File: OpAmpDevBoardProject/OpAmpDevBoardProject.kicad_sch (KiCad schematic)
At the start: 62 parts, among them J101 Conn_01x07, SW101 SW_SPST, SW102 SW_SPST, SW103 SW_SPST, SW104 SW_SPST, SW105 SW_SPST, SW106 SW_SPST, SW107 SW_SPST, SW108 SW_SPST, SW109 SW_SPST, SW110 SW_SPST, SW111 SW_SPST, SW112 SW_SPST, SW113 SW_SPST, SW114 SW_SPST, SW115 SW_SPST, SW116 SW_SPST, SW117 SW_SPST, SW118 SW_SPST, SW119 SW_SPST, SW120 SW_SPST, SW121 SW_SPST, SW122 SW_SPST, SW123 SW_SPST, SW124 SW_SPST, SW125 SW_SPST, SW126 SW_SPST, SW127 SW_SPST, SW128 SW_SPST, SW129 SW_SPST, SW130 SW_SPST, SW131 SW_SPST, SW132 SW_SPST, SW133 SW_SPST, SW134 SW_SPST, SW135 SW_SPST, SW136 SW_SPST, SW137 SW_SPST, SW138 SW_SPST, U101 DoualOutOpAmpGeneric

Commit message: finished botzh sides
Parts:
- added H101, H102, H103, H104: MountingHole, OpampDeVBoard_Foot_Lib:Spacer, symbol Mechanical:MountingHole
- added J102, J103, J104, J105, J106, J107, J108, J112, J113, J114, J115, J117, J118, J119, J120, J122, J123, J124, J125, J126, J127, J128: Conn_01x01_Pin, Connector_PinHeader_2.54mm:PinHeader_1x01_P2.54mm_Vertical, symbol Connector:Conn_01x01_Pin
- added J109: Conn_01x07_Socket, Connector_PinHeader_2.54mm:PinHeader_1x07_P2.54mm_Vertical, symbol Connector:Conn_01x07_Socket
- added J110, J111, J116, J121: 227161-2, OpAmpDevBoard_Mouser:2271612, symbol OpAmpBoard_Mouser:227161-2
- added RV103, RV104, RV106, RV107: R_Potentiometer, OpampDeVBoard_Foot_Lib:PTV09A-1_Vertical, symbol Device:R_Potentiometer
- added SW139, SW140, SW141, SW142, SW143, SW144, SW145, SW146: SW_SPST, OpAmpDevBoard_Mouser:SS12SDP2, symbol Switch:SW_SPST
- C101, C102, C103, C104, C105, C106, C107, C108: footprint (none) -> Capacitor_SMD:C_0805_2012Metric_Pad1.18x1.45mm_HandSolder
- J101: footprint (none) -> Connector_PinSocket_2.54mm:PinSocket_1x07_P2.54mm_Vertical
- R101, R102, R103, R104, R105, R106, R107, R108, R109, R110, R111, R112: footprint (none) -> Resistor_SMD:R_0805_2012Metric_Pad1.20x1.40mm_HandSolder
- RV101, RV102: footprint (none) -> OpampDeVBoard_Foot_Lib:PTV09A-1_Vertical
- SW101, SW102, SW103, SW104, SW105, SW106, SW107, SW108, SW109, SW110, SW111, SW112, SW113, SW114, SW115, SW116, SW117, SW118, SW119, SW120, SW121, SW122, SW123, SW124, SW125, SW126, SW127, SW128, SW129, SW130, SW131, SW132, SW133, SW134, SW135, SW136, SW137, SW138: footprint (none) -> OpAmpDevBoard_Mouser:SS12SDP2
- U101: footprint (none) -> OpampDeVBoard_Foot_Lib:OpAmpBoardConnector
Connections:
- net GND: now also J101.2 (Pin_2), J109.2 (Pin_2), J110.2 (Ground), J110.MH1, J110.MH2, J111.2 (Ground), J111.MH1, J111.MH2, J116.2 (Ground), J116.MH1, J116.MH2, J121.2 (Ground), J121.MH1, J121.MH2, J122.1 (Pin_1), J123.1 (Pin_1), RV103.3, RV104.3, RV106.3, RV107.3
- net at C104.2, R106.2, SW129.2 (B)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: now also J116.1 (Signal), J117.1 (Pin_1), J118.1 (Pin_1)
- net at C101.1, C105.2, R101.1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: now also J102.1 (Pin_1), J107.1 (Pin_1), J108.1 (Pin_1)
- net at R107.1: now also SW141.2 (B); no longer SW133.1 (A)
- net at R107.2, SW117.2 (B), SW118.2 (B)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: now also J105.1 (Pin_1), RV103.2, SW140.1 (A), SW144.1 (A); no longer R108.1
- net at C102.2, C108.1, R112.1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: now also J103.1 (Pin_1), J127.1 (Pin_1), J128.1 (Pin_1)
- net at C102.1, R104.2, SW111.2 (B)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: now also J126.1 (Pin_1), RV107.2
- net at R103.2, SW113.2 (B), SW114.2 (B)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: now also J125.1 (Pin_1), RV106.2, SW143.1 (A), SW146.1 (A); no longer R104.1
- net at C105.1, R108.2, SW119.2 (B)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: now also J106.1 (Pin_1), RV104.2
- net at SW136.1 (A): now also J110.1 (Signal), J112.1 (Pin_1), J113.1 (Pin_1), J124.1 (Pin_1), SW142.1 (A), SW145.1 (A); no longer R103.1
- net at C107.2, R110.2, SW101.2 (B)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: now also J119.1 (Pin_1), J120.1 (Pin_1), J121.1 (Signal)
- net V+: now reaches J101.1 (Pin_1)
- net V+: now also U101.8 (V+), J109.1 (Pin_1)
- net V-: now reaches J101.3 (Pin_3)
- net V-: now also U101.5 (V-), J109.3 (Pin_3)
- net Act: now reaches J101.4 (Pin_4)
- net Act: now also U101.9 (Act), J109.4 (Pin_4)
- net Sleep: now reaches J101.5 (Pin_5)
- net Sleep: now also U101.10 (Sleep), J109.5 (Pin_5)
- net Div1: now reaches J101.6 (Pin_6)
- net Div1: now also U101.3 (Div1), J109.6 (Pin_6)
- net Div2: now reaches J101.7 (Pin_7)
- net Div2: now also U101.4 (Div2), J109.7 (Pin_7)
- new net: RV103.1, SW139.2 (B)
- new net: R108.1, SW144.2 (B)
- new net: J104.1 (Pin_1), J111.1 (Signal), J114.1 (Pin_1), J115.1 (Pin_1), SW133.1 (A), SW139.1 (A), SW141.1 (A)
- new net: R104.1, SW146.2 (B)
- new net: RV104.1, SW140.2 (B)
- new net: RV107.1, SW143.2 (B)
- new net: R103.1, SW145.2 (B)
- new net: RV106.1, SW142.2 (B)
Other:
- moved on the sheet: C101, C102, C103, C104, C105, C106, C107, C108, J101, R101, R102, R103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

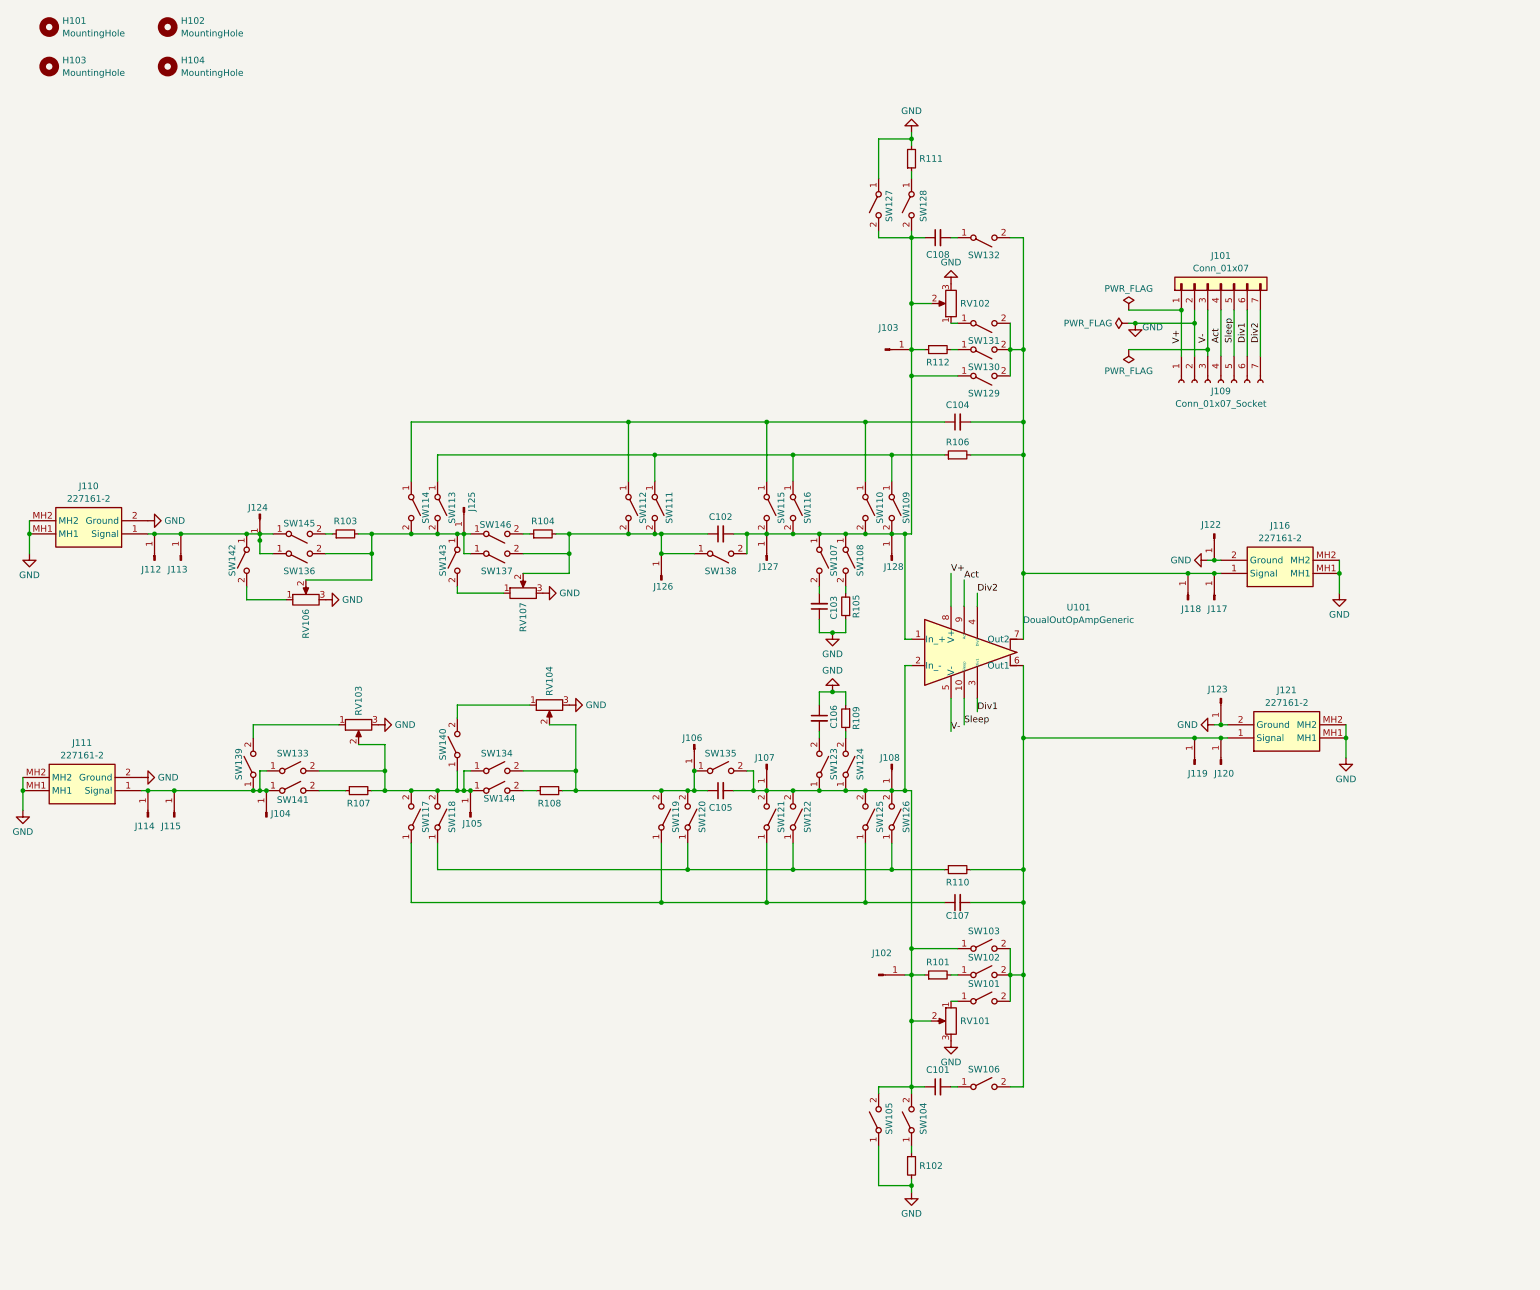
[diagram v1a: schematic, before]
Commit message: added double switch and started changing schematic
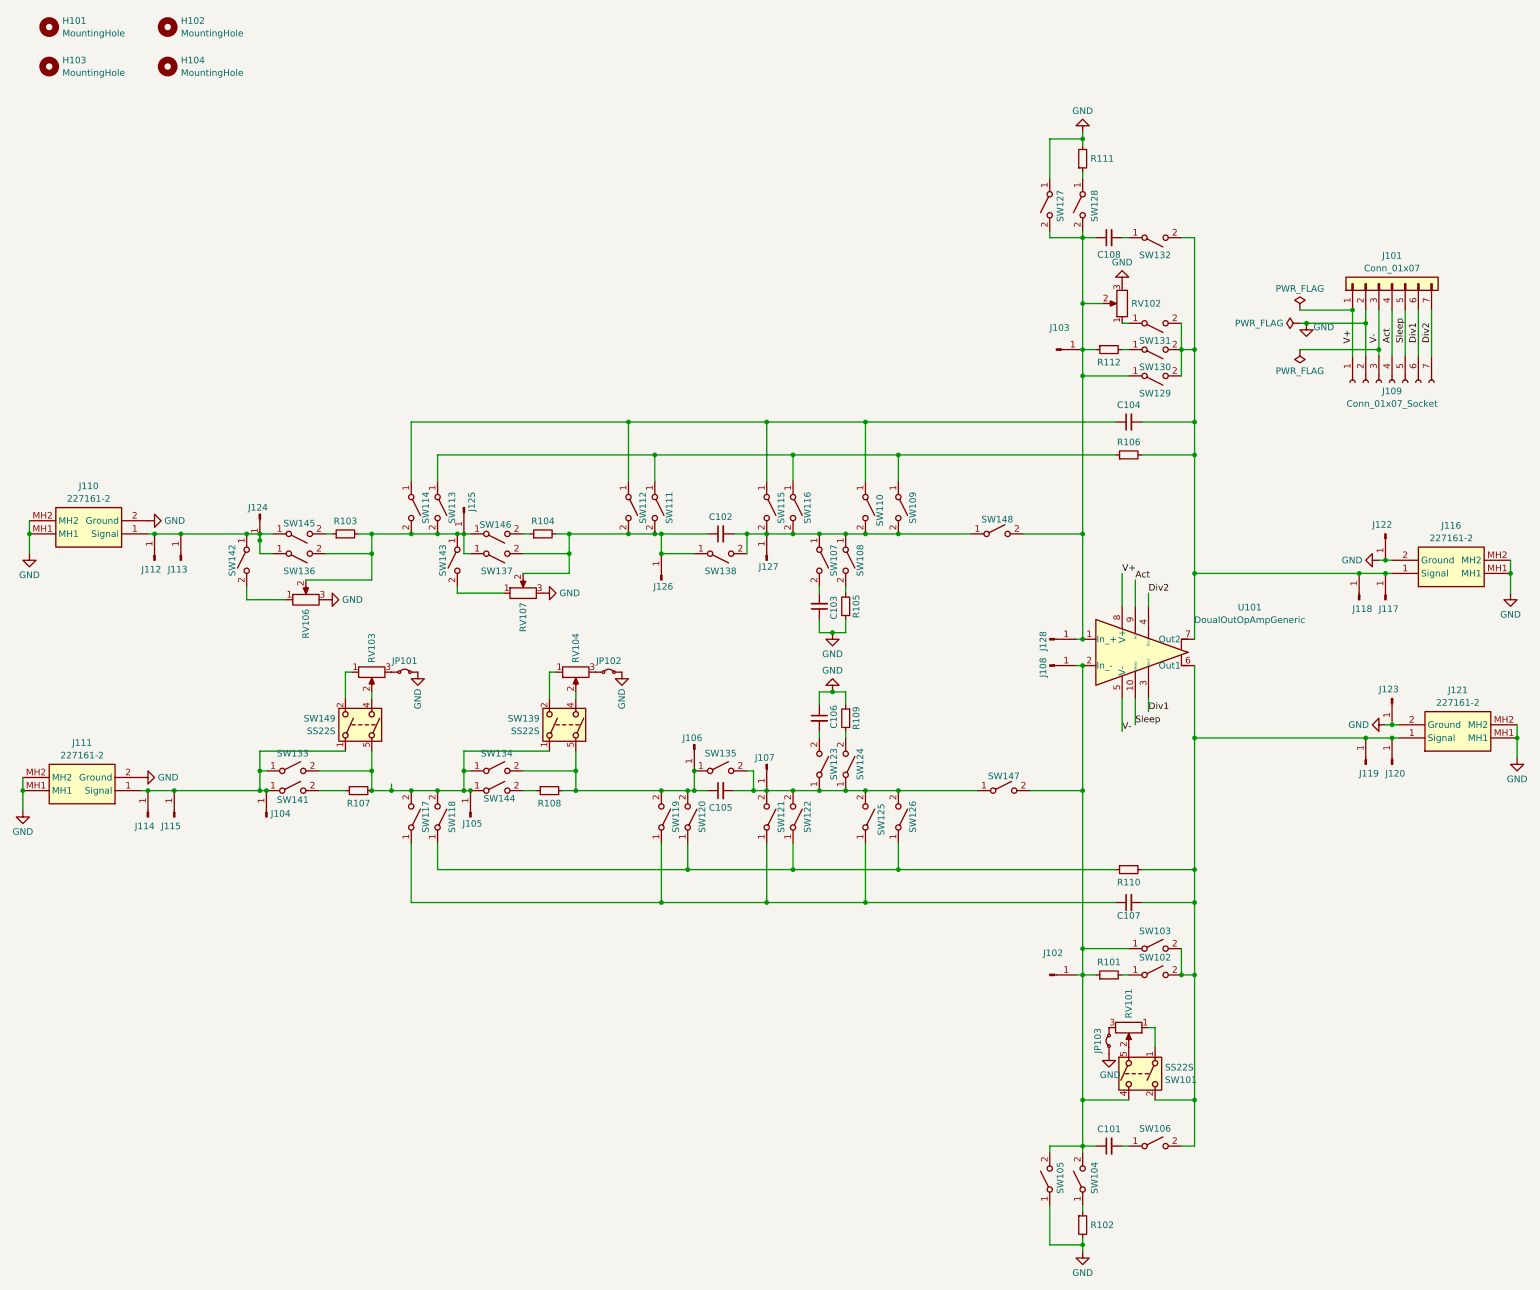
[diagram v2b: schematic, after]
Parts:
- removed SW101, SW139, SW140: SW_SPST, OpAmpDevBoard_Mouser:SS12SDP2, symbol Switch:SW_SPST
- added JP101, JP102, JP103: Jumper_2_Small_Bridged, symbol Jumper:Jumper_2_Small_Bridged
- added SW101, SW139, SW149: SS22S, OpAmpDevBoard_Mouser:SS22SDP2, symbol DiverseOpAmps:SS22S
- added SW147, SW148: SW_SPST, OpAmpDevBoard_Mouser:SS12SDP2, symbol Switch:SW_SPST
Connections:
- net GND: now also JP101.2 (B), JP102.2 (B), JP103.1 (A); no longer RV101.3, RV103.3, RV104.3
- net at C105.2, J107.1 (Pin_1), SW121.2 (B)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: now also SW147.1 (A); no longer C101.1, J102.1 (Pin_1), J108.1 (Pin_1), R101.1, RV101.2, SW103.1 (A), SW104.2 (B), SW105.2 (B), U101.2 (In_-)
- net at C102.2, J127.1 (Pin_1), SW107.1 (A)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: now also SW148.1 (A); no longer C108.1, J103.1 (Pin_1), J128.1 (Pin_1), R112.1, RV102.2, SW127.2 (B), SW128.2 (B), SW129.1 (A), U101.1 (In_+)
- net at J105.1 (Pin_1), R107.2, SW117.2 (B)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: now also SW139.1, SW149.5; no longer RV103.2
- net at C107.2, J119.1 (Pin_1), J120.1 (Pin_1)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: now also SW101.2
- net at RV103.1: now also SW149.2
- net at C105.1, J106.1 (Pin_1), R108.2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: now also SW139.5; no longer RV104.2
- net at RV101.1: now also SW101.1
- net at J104.1 (Pin_1), J111.1 (Signal), J114.1 (Pin_1)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: now also SW149.1
- net at RV104.1: now also SW139.2
- new net: C101.1, J102.1 (Pin_1), J108.1 (Pin_1), R101.1, SW101.4, SW103.1 (A), SW104.2 (B), SW105.2 (B), SW147.2 (B), U101.2 (In_-)
- new net: C108.1, J103.1 (Pin_1), J128.1 (Pin_1), R112.1, RV102.2, SW127.2 (B), SW128.2 (B), SW129.1 (A), SW148.2 (B), U101.1 (In_+)
- new net: RV103.2, SW149.4
- new net: JP101.1 (A), RV103.3
- new net: RV101.2, SW101.5
- new net: JP103.2 (B), RV101.3
- new net: RV104.2, SW139.4
- new net: JP102.1 (A), RV104.3
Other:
- moved on the sheet: C101, C104, C107, C108, J101, J102, J103, J108, J109, J116, J117, J118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

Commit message: late night fu me
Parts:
- removed SW131, SW142, SW143: SW_SPST, OpAmpDevBoard_Mouser:SS12SDP2, symbol Switch:SW_SPST
- added JP104, JP105, JP106: Jumper_2_Small_Bridged, Connector_PinHeader_2.54mm:PinHeader_1x02_P2.54mm_Vertical, symbol Jumper:Jumper_2_Small_Bridged
- added SW131, SW140, SW142: SS22S, OpAmpDevBoard_Mouser:SS22SDP2, symbol DiverseOpAmps:SS22S
- JP101, JP102, JP103: footprint (none) -> Connector_PinHeader_2.54mm:PinHeader_1x02_P2.54mm_Vertical
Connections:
- net GND: now also JP104.2 (B), JP105.2 (B), JP106.1 (A); no longer RV102.3, RV106.3, RV107.3
- net at C104.2, J116.1 (Signal), J117.1 (Pin_1)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: now also SW131.2
- net at C108.1, J103.1 (Pin_1), J128.1 (Pin_1)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: now also SW131.4; no longer RV102.2
- net at C102.1, J126.1 (Pin_1), R104.2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: now also SW142.5; no longer RV107.2
- net at J125.1 (Pin_1), R103.2, SW113.2 (B)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: now also SW140.5, SW142.1; no longer RV106.2
- net at J110.1 (Signal), J112.1 (Pin_1), J113.1 (Pin_1)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: now also SW140.1
- net at RV102.1: now also SW131.1
- net at RV107.1: now also SW142.2
- net at RV106.1: now also SW140.2
- new net: RV107.2, SW142.4
- new net: JP106.2 (B), RV102.3
- new net: RV102.2, SW131.5
- new net: RV106.2, SW140.4
- new net: JP105.1 (A), RV107.3
- new net: JP104.1 (A), RV106.3
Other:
- moved on the sheet: C108, R111, RV102, RV106, RV107, SW127, SW128, SW132

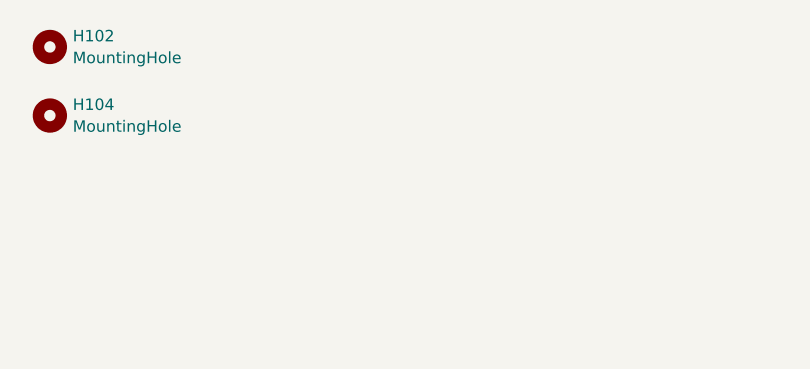
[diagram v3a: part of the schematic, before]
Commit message: added gnd connectors
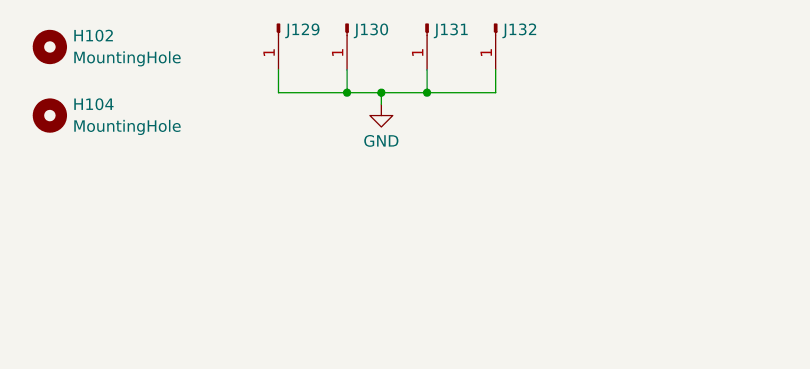
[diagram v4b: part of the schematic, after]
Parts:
- added J129, J130, J131, J132: Conn_01x01_Pin, Connector_PinHeader_2.54mm:PinHeader_1x01_P2.54mm_Vertical, symbol Connector:Conn_01x01_Pin
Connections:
- net GND: now also J129.1 (Pin_1), J130.1 (Pin_1), J131.1 (Pin_1), J132.1 (Pin_1)
